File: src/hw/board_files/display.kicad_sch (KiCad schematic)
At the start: 20 parts, among them U2 7.3inch_E-Ink_Display

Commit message: sch progress
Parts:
- added C18, C24: 4u7, symbol Device:C_Small
- added C19, C22, C23, C25: 10u, symbol Device:C_Small
- added C20, C21, C26: 100n, symbol Device:C_Small
- added D1: BZT52C27, symbol Device:D_Zener
- added D2, D3, D4, D5: MBR0530, symbol Device:D_Schottky
- added L1, L2: 10u, symbol Device:L
- added Q1: SI1308EDL, symbol Simulation_SPICE:NMOS
- added Q2, Q3: SI2301CDS-T1-E3, symbol Simulation_SPICE:PMOS
- added Q4: NPN, symbol Simulation_SPICE:NPN
- added R10: 1k, symbol Device:R_Small_US
- added R11, R8, R9: 47k, symbol Device:R_Small_US
- added R12: 10k, symbol Device:R_Small_US
- added R3, R6: 1M, symbol Device:R_Small_US
- added R4, R7: 0R2, symbol Device:R_Small_US
- added R5: 0R, symbol Device:R_Small_US
- C10, C9: value 10u -> 1u
- C16: value 1u -> 470n
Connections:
- net +3V3: now also C18.1, C18.2, C19.2, C20.2, C21.2, C22.2, C24.1, C24.2, C25.2, C26.2, D1.2 (A), D4.1 (K), L1.1, Q2.1 (D), Q4.3 (E), R11.2, R3.2, R4.1, R6.1, R7.1, R9.2
- net GDRC: now also Q2.2 (G), R6.2
- net GDRH: now also Q1.2 (G), R3.1
- net RESEC: now also L2.1, R7.2
- net RESEH: now also Q1.3 (S), R4.2
- net VGH: now also R5.2
- net VGL: now also C19.1, C20.1, D3.2 (A)
- net VPC: now also C25.1, C26.1, D5.2 (A)
- net VPH: now also C21.1, C22.1, D2.1 (K), R5.1
- new net: Q3.2 (G), Q4.1 (C)
- new net: Q4.2 (B), R12.2, R9.1
- new net: C23.2, D3.1 (K), D4.2 (A)
- new net: C23.1, D1.1 (K), D2.2 (A), L1.2, Q1.1 (D)
- new net: D5.1 (K), L2.2, Q2.3 (S)
- new net: R10.1, R12.1
- new net: R10.2, R11.1

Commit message: Sch progress
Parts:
- removed Q3: SI2301CDS-T1-E3, symbol Simulation_SPICE:PMOS
- removed Q4: NPN, symbol Simulation_SPICE:NPN
- removed R10: 1k, symbol Device:R_Small_US
- removed R11, R8, R9: 47k, symbol Device:R_Small_US
- removed R12: 10k, symbol Device:R_Small_US
- added C7: DNP, symbol Device:C_Small
- added C8: 100n, symbol Device:C_Small
- added R18: 0R, symbol Device:R_Small_US
- added U4: TPS22917DBVR, Package_TO_SOT_SMD:SOT-23-6, symbol Power_Management:TPS22917DBV
- renumbered C2 to C10, C18 to C11, C23 to C12, C21 to C13, C22 to C14, C3 to C15, C19 to C16, C20 to C17, C4 to C18, C5 to C19, C6 to C20, C7 to C21, C8 to C22, C9 to C23, C10 to C24, C24 to C25, C15 to C26, C25 to C27, C26 to C28, C12 to C29, C17 to C30, C11 to C31, C13 to C32, C14 to C33, C16 to C34, C1 to C9, D2 to D4, D1 to D5, D3 to D6, D4 to D7, D5 to D8, R1 to R19, R5 to R20, R3 to R21, R4 to R22, R6 to R23, R7 to R24, R2 to R25, U2 to U5
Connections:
- net +3V3: now also C7.1, C8.2, U4.1 (VIN); no longer C10.2, C11.1, C11.2, C13.2, C14.2, C15.2, C16.2, C17.2, C18.2, C19.2, C20.2, C21.2, C22.2, C23.2, C24.2, C25.1, C25.2, C26.2, C27.2, C28.2, C29.2, C30.1, C30.2, C32.2, C34.2, C9.1, C9.2, D5.2 (A), D7.1 (K), L1.1, Q2.1 (D), R19.1, R21.2, R22.1, R23.1, R24.1, U5.12 (GNDA+(GND)), U5.2 (TFT_VCOM), U5.21 (GNDA+(GND)), U5.27 (BS1), U5.3 (FPL_VCOM), U5.38 (VDD), U5.39 (GNDA/GND), U5.4 (VDD), U5.40 (VDDIO), U5.8 (RESEL), U5.MP
- new net: C7.2, U4.4 (CT)
- new net: R18.2, U4.5 (QOD)
- new net +3V3_EPD: C10.2, C11.1, C11.2, C13.2, C14.2, C15.2, C16.2, C17.2, C18.2, C19.2, C20.2, C21.2, C22.2, C23.2, C24.2, C25.1, C25.2, C26.2, C27.2, C28.2, C29.2, C30.1, C30.2, C32.2, C34.2, C8.1, C9.1, C9.2, D5.2 (A), D7.1 (K), L1.1, Q2.1 (D), R18.1, R19.1, R21.2, R22.1, R23.1, R24.1, U4.2 (GND), U4.6 (VOUT), U5.12 (GNDA+(GND)), U5.2 (TFT_VCOM), U5.21 (GNDA+(GND)), U5.27 (BS1), U5.3 (FPL_VCOM), U5.38 (VDD), U5.39 (GNDA/GND), U5.4 (VDD), U5.40 (VDDIO), U5.8 (RESEL), U5.MP
- new net EPD_EN: U4.3 (ON)
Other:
- note added: "E-Ink Display"
- moved on the sheet: C10, C11, C12, C13, C14, C15, C16, C17, C18, C19, C20, C21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

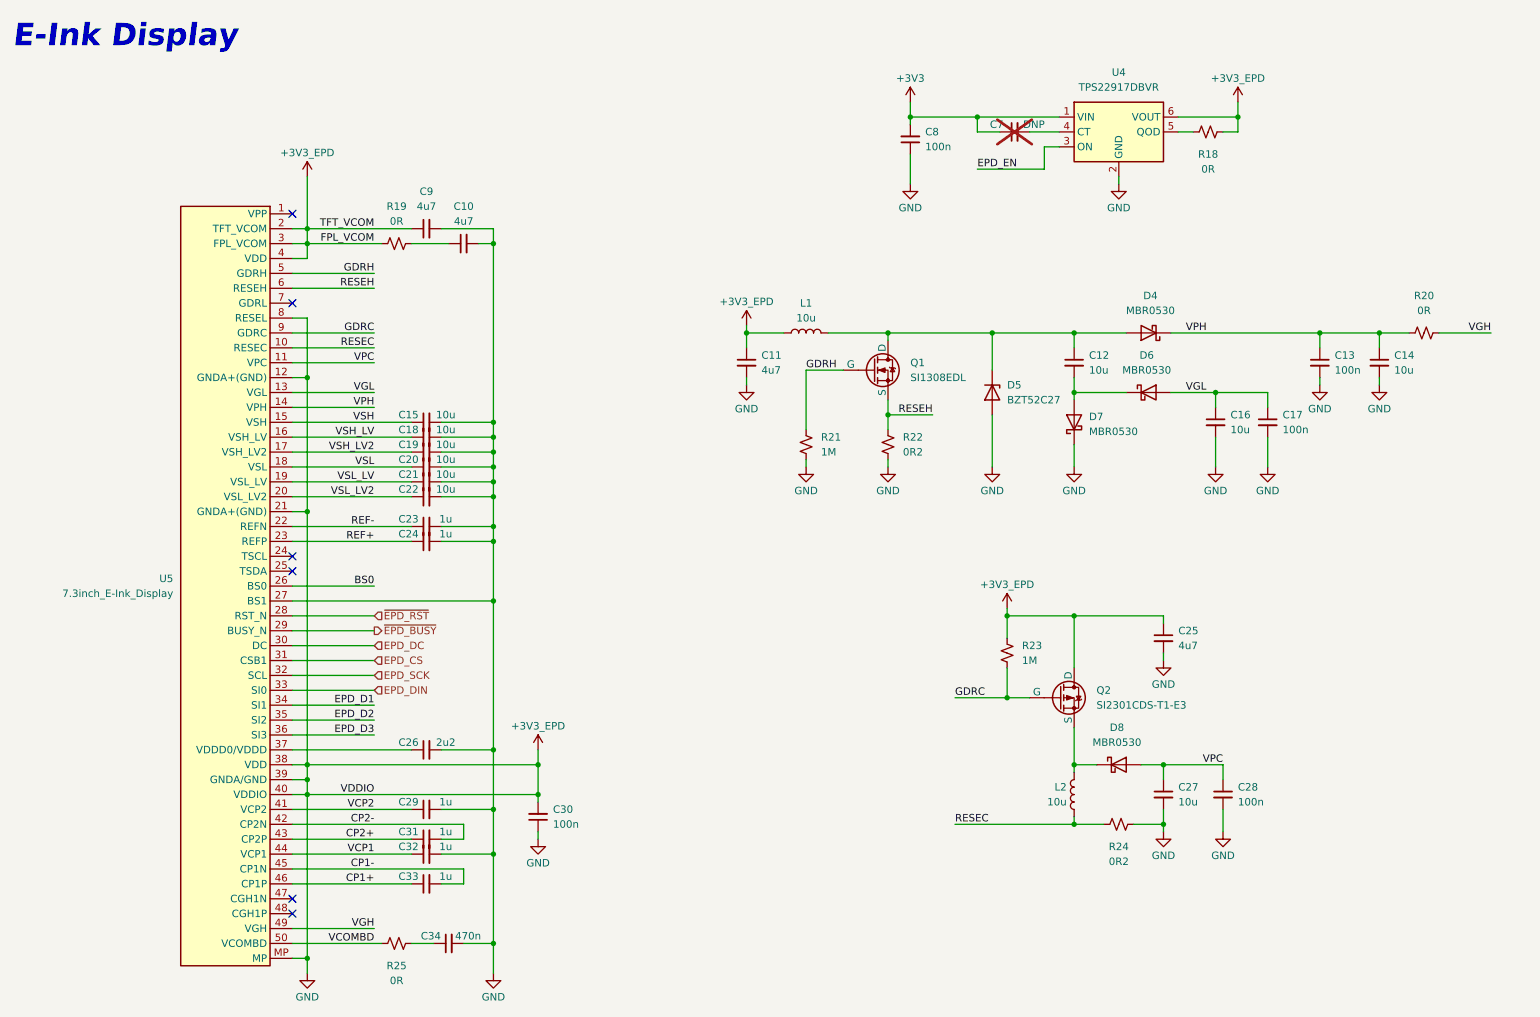
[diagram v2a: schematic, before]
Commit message: Schematic almost done. Assigning footprints
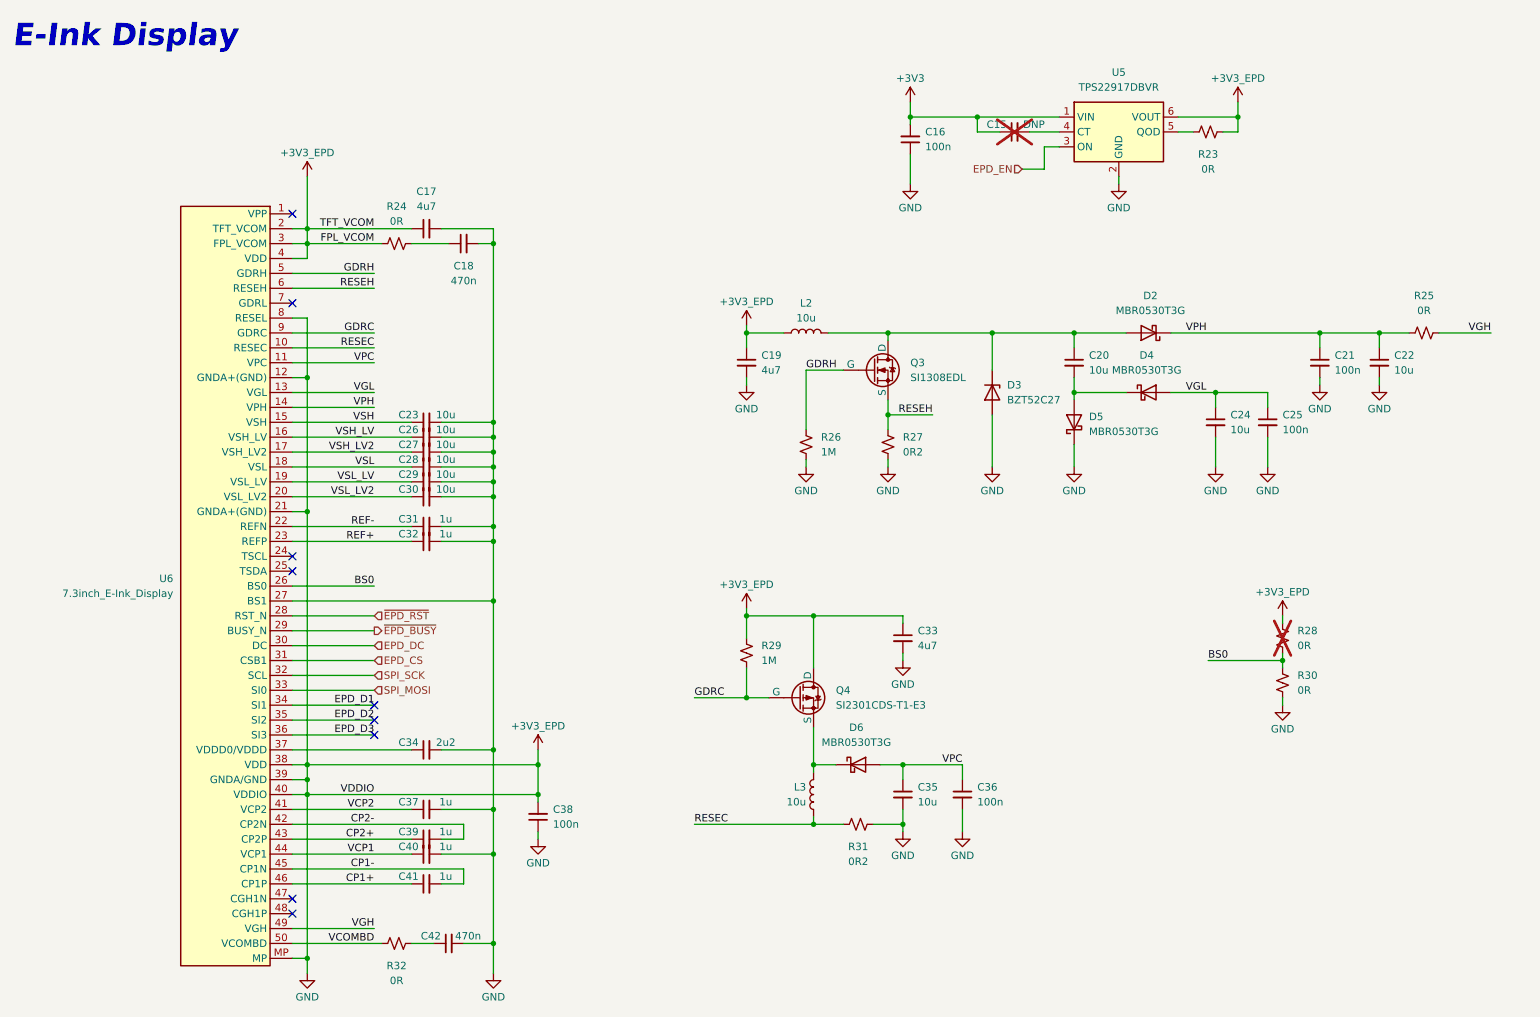
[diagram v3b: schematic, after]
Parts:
- added R28, R30: 0R, symbol Device:R_Small_US
- C15: renamed from C7; footprint (none) -> Capacitor_SMD:C_0603_1608Metric_Pad1.08x0.95mm_HandSolder
- C16: renamed from C8; footprint (none) -> Capacitor_SMD:C_0603_1608Metric_Pad1.08x0.95mm_HandSolder
- C17: renamed from C9; footprint (none) -> Capacitor_SMD:C_0805_2012Metric_Pad1.18x1.45mm_HandSolder
- C18: renamed from C10; value 4u7 -> 470n; footprint (none) -> Capacitor_SMD:C_0603_1608Metric_Pad1.08x0.95mm_HandSolder
- C19: renamed from C11; footprint (none) -> Capacitor_SMD:C_0805_2012Metric_Pad1.18x1.45mm_HandSolder
- C20: renamed from C12; footprint (none) -> Capacitor_SMD:C_0805_2012Metric_Pad1.18x1.45mm_HandSolder
- C21: renamed from C13; footprint (none) -> Capacitor_SMD:C_0603_1608Metric_Pad1.08x0.95mm_HandSolder
- C22: renamed from C14; footprint (none) -> Capacitor_SMD:C_0805_2012Metric_Pad1.18x1.45mm_HandSolder
- C23: renamed from C15; footprint (none) -> Capacitor_SMD:C_0805_2012Metric_Pad1.18x1.45mm_HandSolder
- C24: renamed from C16; footprint (none) -> Capacitor_SMD:C_0805_2012Metric_Pad1.18x1.45mm_HandSolder
- C25: renamed from C17; footprint (none) -> Capacitor_SMD:C_0603_1608Metric_Pad1.08x0.95mm_HandSolder
- C26: renamed from C18; footprint (none) -> Capacitor_SMD:C_0805_2012Metric_Pad1.18x1.45mm_HandSolder
- C27: renamed from C19; footprint (none) -> Capacitor_SMD:C_0805_2012Metric_Pad1.18x1.45mm_HandSolder
- C28: renamed from C20; footprint (none) -> Capacitor_SMD:C_0805_2012Metric_Pad1.18x1.45mm_HandSolder
- C29: renamed from C21; footprint (none) -> Capacitor_SMD:C_0805_2012Metric_Pad1.18x1.45mm_HandSolder
- C30: renamed from C22; footprint (none) -> Capacitor_SMD:C_0805_2012Metric_Pad1.18x1.45mm_HandSolder
- C31: renamed from C23; footprint (none) -> Capacitor_SMD:C_0603_1608Metric_Pad1.08x0.95mm_HandSolder
- C32: renamed from C24; footprint (none) -> Capacitor_SMD:C_0603_1608Metric_Pad1.08x0.95mm_HandSolder
- C33: renamed from C25; footprint (none) -> Capacitor_SMD:C_0805_2012Metric_Pad1.18x1.45mm_HandSolder
- C34: renamed from C26; footprint (none) -> Capacitor_SMD:C_0603_1608Metric_Pad1.08x0.95mm_HandSolder
- C35: renamed from C27; footprint (none) -> Capacitor_SMD:C_0805_2012Metric_Pad1.18x1.45mm_HandSolder
- C36: renamed from C28; footprint (none) -> Capacitor_SMD:C_0603_1608Metric_Pad1.08x0.95mm_HandSolder
- C37: renamed from C29; footprint (none) -> Capacitor_SMD:C_0603_1608Metric_Pad1.08x0.95mm_HandSolder
- C38: renamed from C30; footprint (none) -> Capacitor_SMD:C_0603_1608Metric_Pad1.08x0.95mm_HandSolder
- C39: renamed from C31; footprint (none) -> Capacitor_SMD:C_0603_1608Metric_Pad1.08x0.95mm_HandSolder
- C40: renamed from C32; footprint (none) -> Capacitor_SMD:C_0603_1608Metric_Pad1.08x0.95mm_HandSolder
- C41: renamed from C33; footprint (none) -> Capacitor_SMD:C_0603_1608Metric_Pad1.08x0.95mm_HandSolder
- C42: renamed from C34; footprint (none) -> Capacitor_SMD:C_0603_1608Metric_Pad1.08x0.95mm_HandSolder
- D2: renamed from D4; value MBR0530 -> MBR0530T3G; footprint (none) -> Diode_SMD:D_SOD-123
- D3: renamed from D5; footprint (none) -> Diode_SMD:D_SOD-123F
- D4: renamed from D6; value MBR0530 -> MBR0530T3G; footprint (none) -> Diode_SMD:D_SOD-123
- D5: renamed from D7; value MBR0530 -> MBR0530T3G; footprint (none) -> Diode_SMD:D_SOD-123
- D6: renamed from D8; value MBR0530 -> MBR0530T3G; footprint (none) -> Diode_SMD:D_SOD-123
- L2: renamed from L1; footprint (none) -> Inductor_SMD:L_Bourns_SRN6045TA
- L3: renamed from L2; footprint (none) -> Inductor_SMD:L_Bourns_SRN6045TA
- renumbered Q1 to Q3, Q2 to Q4, R18 to R23, R19 to R24, R20 to R25, R21 to R26, R22 to R27, R23 to R29, R24 to R31, R25 to R32, U4 to U5, U5 to U6
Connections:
- net +3V3_EPD: now also R28.2, R30.1
- net BS0: now also R28.1, R30.2
- net EPD_DIN renamed SPI_MOSI
- net EPD_SCK renamed SPI_SCK
- no-connect marks 6 -> 9
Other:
- moved on the sheet: C33, C35, C36, D6, L3, Q4, R29, R31

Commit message: Schematic done. Started layout
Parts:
- removed Q3: SI1308EDL, symbol Simulation_SPICE:NMOS
- added Q3: Si1308EDL, Package_TO_SOT_SMD:SOT-323_SC-70, symbol Transistor_FET:Si1308EDL
- Q4: footprint (none) -> Package_TO_SOT_SMD:SOT-23
- R23, R24, R25, R27, R28, R30, R31, R32: footprint (none) -> Resistor_SMD:R_0603_1608Metric_Pad0.98x0.95mm_HandSolder
- R26, R29: footprint (none) -> Resistor_SMD:R_0805_2012Metric_Pad1.20x1.40mm_HandSolder
- renumbered C15 to C18, C16 to C19, C17 to C20, C18 to C21, C19 to C22, C20 to C23, C21 to C24, C22 to C25, C23 to C26, C24 to C27, C25 to C28, C26 to C29, C27 to C30, C28 to C31, C29 to C32, C30 to C33, C31 to C34, C32 to C35, C33 to C36, C34 to C37, C35 to C38, C36 to C39, C37 to C40, C38 to C41, C39 to C42, C40 to C43, C41 to C44, C42 to C45
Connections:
- net EPD_D2 is gone; now on net GND: U6.35 (SI2)
- net EPD_D3 is gone; now on net GND: U6.36 (SI3)
- net +3V3_EPD: now also Q4.3 (D); no longer C19.1, C20.1, C20.2, C21.2, C22.2, C24.2, C25.2, C26.2, C27.2, C28.2, C29.2, C30.2, C31.2, C32.2, C33.2, C34.2, C35.2, C36.2, C37.2, C38.2, C39.2, C40.2, C41.1, C43.2, C45.2, D3.2 (A), D5.1 (K), Q4.1 (D), R24.1, R26.2, R27.1, R30.1, R31.1, U5.2 (GND), U6.12 (GNDA+(GND)), U6.2 (TFT_VCOM), U6.21 (GNDA+(GND)), U6.27 (BS1), U6.3 (FPL_VCOM), U6.39 (GNDA/GND), U6.8 (RESEL), U6.MP
- net GDRC: now also Q4.1 (G); no longer Q4.2 (G)
- net GDRH: now also Q3.1 (G)
- net RESEH: now also Q3.2 (S)
- net at C23.1, D2.2 (A), D3.1 (K)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: now also Q3.3 (D)
- net at D6.1 (K), L3.2: now also Q4.2 (S); no longer Q4.3 (S)
- net EPD_D1 renamed GND
- net GND: now also C19.1, C20.2, C21.2, C22.2, C24.2, C25.2, C26.2, C27.2, C28.2, C29.2, C30.2, C31.2, C32.2, C33.2, C34.2, C35.2, C36.2, C37.2, C38.2, C39.2, C40.2, C41.1, C43.2, C45.2, D3.2 (A), D5.1 (K), R26.2, R27.1, R30.1, R31.1, U5.2 (GND), U6.12 (GNDA+(GND)), U6.21 (GNDA+(GND)), U6.27 (BS1), U6.39 (GNDA/GND), U6.8 (RESEL), U6.MP
- new net FPL_VCOM: R24.1, U6.3 (FPL_VCOM)
- new net TFT_VCOM: C20.1, U6.2 (TFT_VCOM)
- no-connect marks 9 -> 6

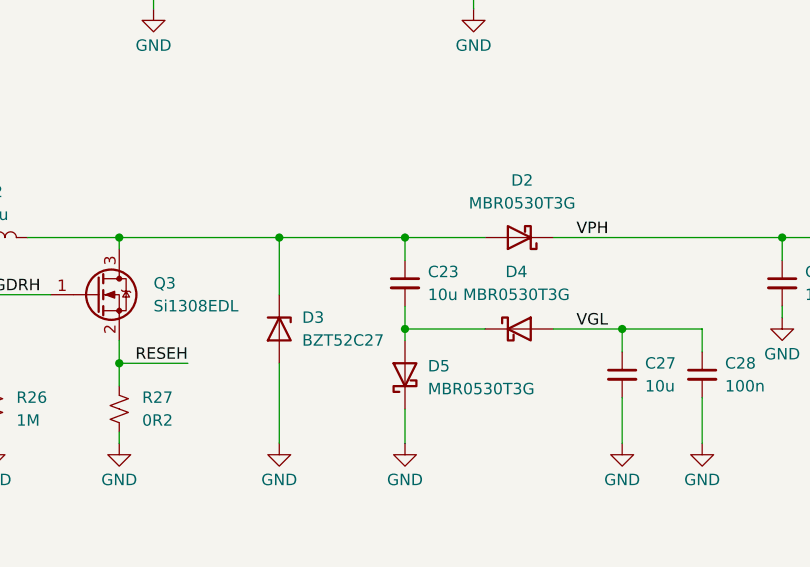
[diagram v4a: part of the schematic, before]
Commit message: Started display circuit layout
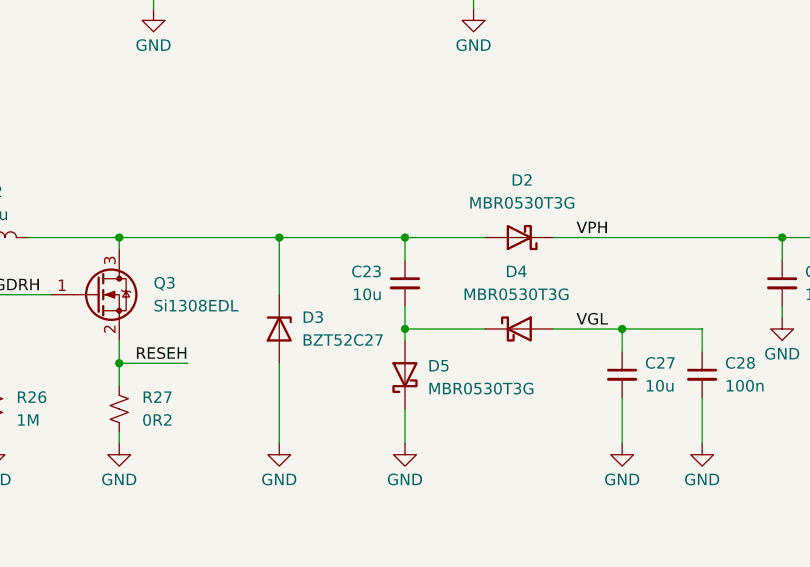
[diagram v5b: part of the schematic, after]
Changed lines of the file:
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@@
 		(fields_autoplaced yes)
 		(property "Reference" "C23"
-			(at 196.85 71.1262 0)
+			(at 191.77 71.1262 0)
 			(effects
 				(font
 					(size 1.27 1.27)
 				)
-				(justify left)
+				(justify right)
 			)
 		)
 		(property "Value" "10u"
-			(at 196.85 73.6662 0)
+			(at 191.77 73.6662 0)
 			(effects
 				(font
 					(size 1.27 1.27)
 				)
-				(justify left)
+				(justify right)
 			)
 		)
